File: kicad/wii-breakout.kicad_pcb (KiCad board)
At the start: 2 copper layers, 21.1 x 75.5 mm, 11 parts, among them J1 Data Header, J2 USB, J3 BT, J4 GameCube, J5 Reset, J6 Audio Header, J7 Video Header, J8 Audio, J9 Video

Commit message: v1.0
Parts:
- removed the J6 at (88.8, 97.9)
- removed the J7 at (88.8, 109.2)
- added J3: Video, Connector_JST:JST_SH_BM04B-SRSS-TB_1x04-1MP_P1.00mm_Vertical, F.Cu at (82.3, 101.3)
- added J5: GameCube, TestPoint:TestPoint_4Pads_2.0x1.0mm, F.Cu at (86.3, 43.5)
- H1, H2: renamed from REF**; value MountingHole_2.7mm_M2.5_Pad_Via -> MountingHole_Pad
- J1: value Data Header -> Peripherals
- J2: value USB -> Audio; footprint TestPoint:TestPoint_2Pads_2.0x1.0mm -> Connector_JST:JST_SH_BM03B-SRSS-TB_1x03-1MP_P1.00mm_Vertical
- J4: value GameCube -> USB; footprint TestPoint:TestPoint_4Pads_2.0x1.0mm -> TestPoint:TestPoint_2Pads_2.0x1.0mm
- J7: renamed from J3; value BT -> Bluetooth
- J8: footprint TestPoint:TestPoint_2Pads_2.0x1.0mm -> TestPoint:TestPoint_3Pads_2.0x1.0mm
- J9: footprint TestPoint:TestPoint_3Pads_2.0x1.0mm -> TestPoint:TestPoint_4Pads_2.0x1.0mm
- moved J2 44.4 mm to (82.3, 86.2), turned to 90 degrees
- moved J4 8.05 mm to (94.8, 43.5)
- moved J1 6.49 mm to (82.3, 68.0), turned to 90 degrees
- moved J9 3.30 mm to (96.7, 112.5)
- moved J8 2.25 mm to (96.7, 100.2)
- moved J6 0.75 mm to (78.8, 43.5)
- moved J7 0.05 mm to (77.6, 51.0)
- renumbered J5 to J6
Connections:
- H1 pad 1: (no net) -> GND
- H2 pad 1: (no net) -> GND
- J2 pad 1: /USB_D+ -> /AUDIO_LEFT
- J2 pad 2: /USB_D- -> /AUDIO_RIGHT
- J4 pad 1: /GC_4 -> /USB_D+
- J4 pad 2: /GC_3 -> /USB_D-
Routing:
- net /AUDIO_GND: track 0.00 -> 22.4 mm
- net /VIDEO_GND: track 0.00 -> 17.6 mm
- net /AUDIO_LEFT: track 6.68 -> 22.9 mm
- net /AUDIO_RIGHT: track 6.68 -> 22.5 mm
- net /VIDEO_Y: track 7.41 -> 19.1 mm
- net /VIDEO_PB: track 6.62 -> 17.9 mm
- net /USB_D-: track 22.5 -> 33.7 mm
- net /USB_D+: track 22.5 -> 33.7 mm
- net /GC_4: track 18.5 -> 29.3 mm
- net Net-(J1-PadMP): track 0.00 -> 10.6 mm
- net /VIDEO_PR: track 7.33 -> 17.5 mm
- net /GC_3: track 18.0 -> 27.4 mm
- net /BT_D-: track 10.2 -> 18.8 mm
- net /GC_2: track 18.4 -> 26.7 mm
- net /BT_D+: track 11.4 -> 18.8 mm
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- added copper zone on B.Cu, net GND
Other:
- outline, holes or cut-outs redrawn
- board text added: "Wii Breakout v1.0 - @loopj"
- board text added: "⏚"

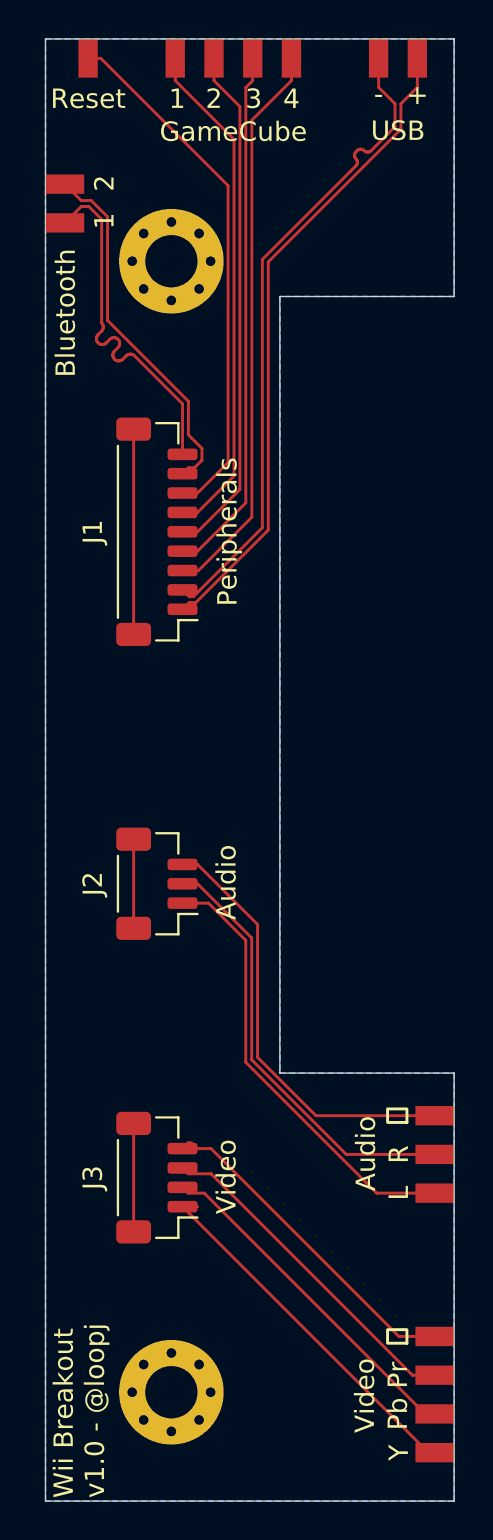
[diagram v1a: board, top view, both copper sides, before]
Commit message: Shrink the board
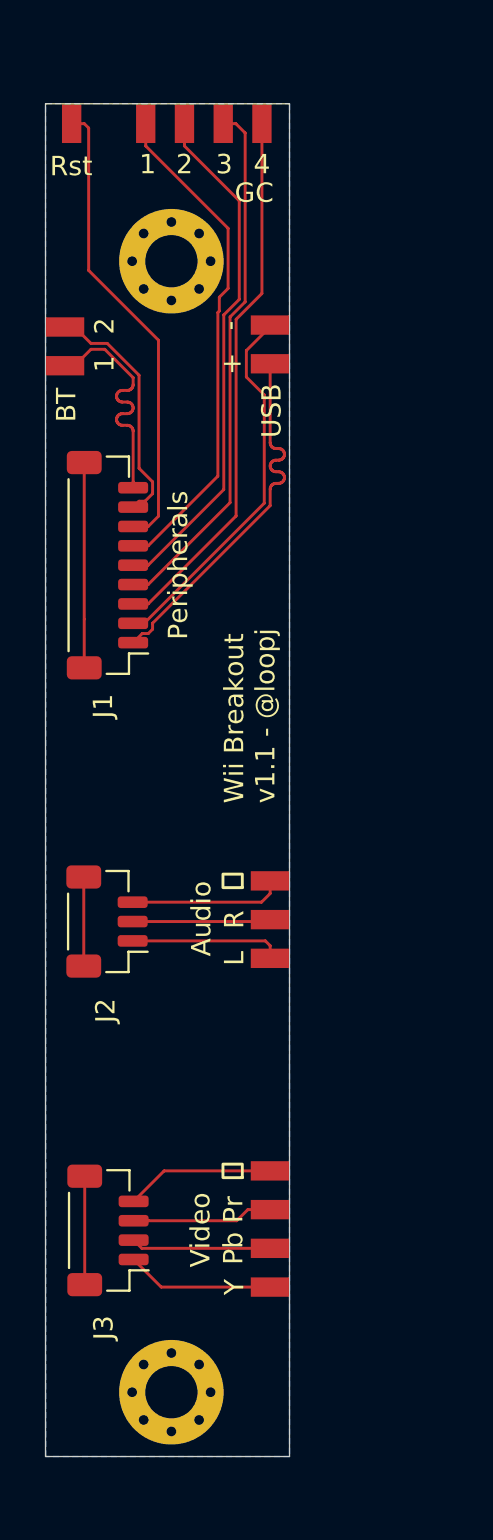
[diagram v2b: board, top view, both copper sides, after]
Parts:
- J5: value GameCube -> GC
- J6: value Reset -> Rst
- J7: value Bluetooth -> BT
- moved J4 16.2 mm to (88.2, 58.3), turned to 180 degrees
- moved J8 14.8 mm to (88.2, 88.0)
- moved J9 12.1 mm to (88.2, 104.0)
- moved J7 7.38 mm to (77.6, 58.4)
- moved J3 3.72 mm to (79.8, 104.1)
- moved J5 3.70 mm to (84.8, 46.9)
- moved J6 3.48 mm to (78.0, 46.9)
- moved J2 3.23 mm to (79.8, 88.1)
- moved J1 3.08 mm to (79.8, 69.7)
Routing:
- net /AUDIO_RIGHT: track 22.5 -> 7.14 mm
- net /AUDIO_LEFT: track 22.9 -> 7.85 mm
- net /AUDIO_GND: track 22.4 -> 7.94 mm
- net /USB_D-: track 33.7 -> 19.4 mm
- net /USB_D+: track 33.7 -> 19.4 mm
- net /VIDEO_Y: track 19.1 -> 7.64 mm
- net /VIDEO_PB: track 17.9 -> 7.23 mm
- net /VIDEO_PR: track 17.5 -> 7.29 mm
- net /VIDEO_GND: track 17.6 -> 7.70 mm
- net /BT_D+: track 18.8 -> 12.6 mm
- net /BT_D-: track 18.8 -> 12.6 mm
- net /RST: track 27.3 -> 24.0 mm
- net /GC_4: track 29.3 -> 28.0 mm
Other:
- board size 21.1 x 75.5 mm -> 12.6 x 69.8 mm
- board text added: "Wii Breakout v1.1 - @loopj"
- board text removed: "Wii Breakout v1.0 - @loopj"

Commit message: v2.0
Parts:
- added J10: ⏚, project-footprints:TestPoint_Pad_2.0x1.0mm, F.Cu at (49.0, 107.6)
- J4, J7: footprint TestPoint:TestPoint_2Pads_2.0x1.0mm -> project-footprints:TestPoint_2Pads_2.0x1.0mm
- J5: footprint TestPoint:TestPoint_4Pads_2.0x1.0mm -> project-footprints:TestPoint_4Pads_2.0x1.0mm
- J6: value Rst -> Reset; footprint TestPoint:TestPoint_Pad_2.0x1.0mm -> project-footprints:TestPoint_Pad_2.0x1.0mm
- J8: footprint TestPoint:TestPoint_3Pads_2.0x1.0mm -> project-footprints:TestPoint_2Pads_2.0x1.0mm
- J9: footprint TestPoint:TestPoint_4Pads_2.0x1.0mm -> project-footprints:TestPoint_3Pads_2.0x1.0mm
- moved J6 60.7 mm to (80.9, 107.6), turned to 90 degrees
- moved J5 54.3 mm to (80.8, 101.1)
- moved H1 51.4 mm to (93.4, 104.4), turned to 270 degrees
- moved J4 49.3 mm to (89.5, 107.6), turned to 90 degrees
- moved H2 48.8 mm to (35.0, 104.4), turned to 270 degrees
- moved J9 45.0 mm to (43.3, 107.6), turned to 90 degrees
- moved J7 44.3 mm to (89.5, 101.1), turned to 270 degrees
- moved J8 39.8 mm to (53.6, 107.6), turned to 90 degrees
- moved J3 36.5 mm to (43.3, 102.2), turned to 0 degrees
- moved J1 35.1 mm to (66.5, 102.2), turned to 0 degrees
- moved J2 29.7 mm to (53.6, 102.2), turned to 0 degrees
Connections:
- J2 pad 3: /AUDIO_GND -> GND
- J3 pad 4: /VIDEO_GND -> GND
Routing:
- net /GC_1: track 26.0 -> 13.1 mm, vias 0 -> 2
- net /BT_D-: track 12.6 -> 23.2 mm
- net /BT_D+: track 12.6 -> 23.2 mm
- net /GC_2: track 26.7 -> 16.5 mm, vias 0 -> 2
- net /USB_D+: track 19.4 -> 29.3 mm
- net /USB_D-: track 19.4 -> 29.1 mm
- net /AUDIO_GND: track 7.94 -> 0.00 mm
- net /GC_3: track 27.5 -> 19.6 mm, vias 0 -> 2
- net /VIDEO_GND: track 7.70 -> 0.00 mm
- net /RST: track 24.0 -> 31.4 mm
- net /GC_4: track 28.0 -> 22.9 mm, vias 0 -> 2
- net /AUDIO_LEFT: track 7.85 -> 4.07 mm
- net GND: track 0.00 -> 3.46 mm, vias 0 -> 3
- net /VIDEO_Y: track 7.64 -> 4.29 mm
- net /VIDEO_PB: track 7.23 -> 4.27 mm
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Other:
- board size 12.6 x 69.8 mm -> 64.5 x 8.5 mm
- board text added: "@loopj"
- board text added: "Wii Breakout"
- board text added: "v2.0"
- board text removed: "Wii Breakout v1.1 - @loopj"
- board text removed: "⏚"

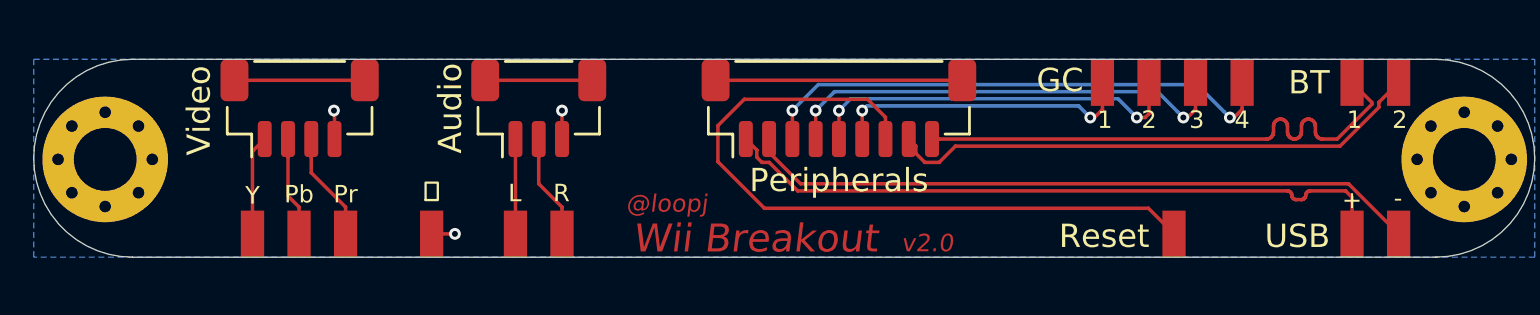
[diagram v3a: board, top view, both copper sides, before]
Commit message: Include mobo power on breakout
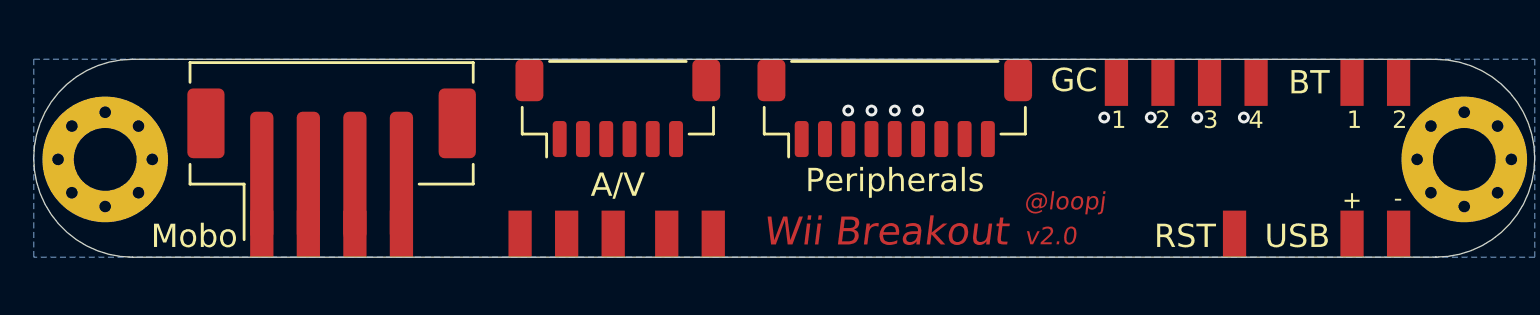
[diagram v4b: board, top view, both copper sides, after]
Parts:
- J10: value ⏚ -> Conn_01x04_Male; footprint project-footprints:TestPoint_Pad_2.0x1.0mm -> project-footprints:TestPoint_4Pads_2.0x1.0mm
- J2: value Audio -> A/V; footprint Connector_JST:JST_SH_BM03B-SRSS-TB_1x03-1MP_P1.00mm_Vertical -> Connector_JST:JST_SH_BM06B-SRSS-TB_1x06-1MP_P1.00mm_Vertical
- J3: value Video -> Mobo; footprint Connector_JST:JST_SH_BM04B-SRSS-TB_1x04-1MP_P1.00mm_Vertical -> Connector_JST:JST_PH_B4B-PH-SM4-TB_1x04-1MP_P2.00mm_Vertical
- J6: value Reset -> RST
- moved J9 11.5 mm to (54.8, 107.6)
- moved J8 6.50 mm to (60.1, 107.6)
- moved J10 4.30 mm to (44.7, 107.6)
- moved J2 3.40 mm to (57.0, 102.2)
- moved J3 2.77 mm to (44.7, 104.6)
- moved J6 2.60 mm to (83.5, 107.6)
- moved J1 2.40 mm to (68.9, 102.2)
- moved J5 0.60 mm to (81.4, 101.1)
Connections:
- J10 pad 1: GND -> /3V3
- J2 pad 1: /AUDIO_LEFT -> /VIDEO_Y
- J2 pad 2: /AUDIO_RIGHT -> /VIDEO_PB
- J2 pad 3: GND -> /VIDEO_PR
- J3 pad 1: /VIDEO_Y -> /3V3
- J3 pad 2: /VIDEO_PB -> /1V15
- J3 pad 3: /VIDEO_PR -> /1V0
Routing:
- net /RST: track 31.4 -> 0.00 mm
- net /USB_D+: track 29.3 -> 0.00 mm
- net /USB_D-: track 29.1 -> 0.00 mm
- net /BT_D-: track 23.2 -> 0.00 mm
- net /BT_D+: track 23.2 -> 0.00 mm
- net /GC_4: track 22.9 -> 0.00 mm, vias 2 -> 1
- net /GC_3: track 19.6 -> 0.00 mm, vias 2 -> 1
- net /GC_2: track 16.5 -> 0.00 mm, vias 2 -> 1
- net /GC_1: track 13.1 -> 0.00 mm, vias 2 -> 1
- net Net-(J1-PadMP): track 10.6 -> 0.00 mm
- net Net-(J3-PadMP): track 5.60 -> 0.00 mm
- net /VIDEO_PR: track 4.69 -> 0.00 mm
- net Net-(J2-PadMP): track 4.60 -> 0.00 mm
- net /AUDIO_RIGHT: track 4.49 -> 0.00 mm
- net /VIDEO_Y: track 4.29 -> 0.00 mm
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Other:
- board text removed: "L"
- board text removed: "Pb"
- board text removed: "Pr"
- board text removed: "R"
- board text removed: "Y"
